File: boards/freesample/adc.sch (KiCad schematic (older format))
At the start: 20 parts, among them U41 DS25BR150, U8 HMC675LP3E

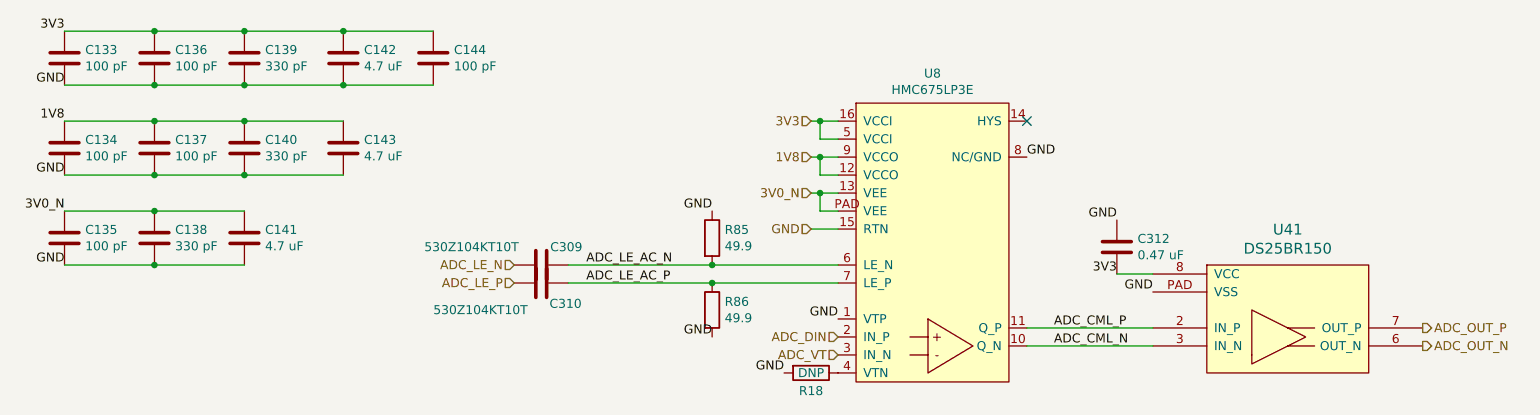
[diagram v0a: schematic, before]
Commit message: Added more test points. Started picking packages for passives. Continued schematic review.
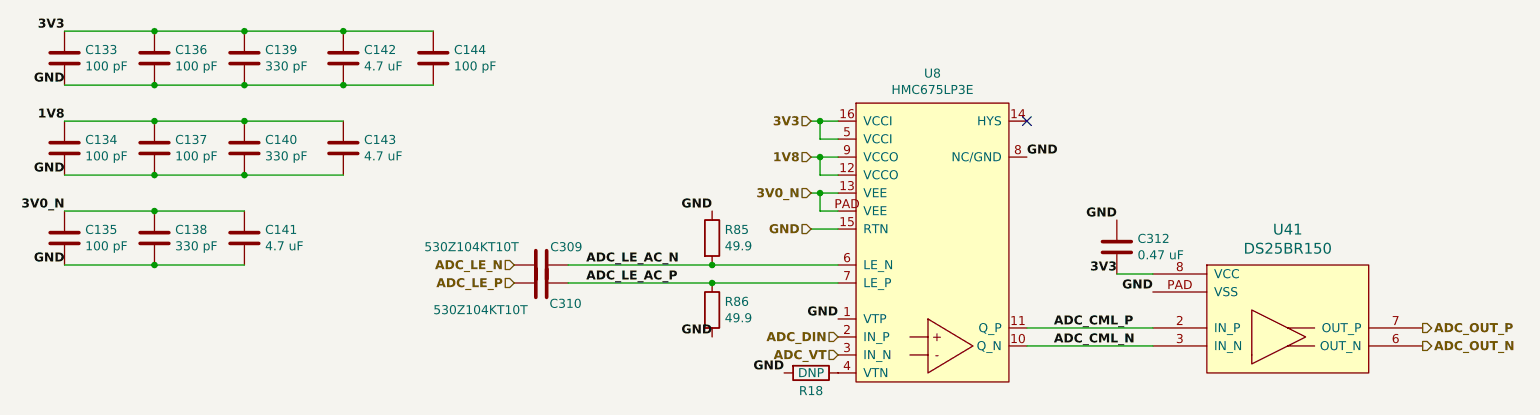
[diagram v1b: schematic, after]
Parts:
- C133, C134, C135, C136, C137, C138, C139, C140, C144, C309, C310: footprint (none) -> azonenberg_pcb:EIA_0201_CAP_NOSILK
- C141, C142, C143: footprint (none) -> azonenberg_pcb:EIA_0603_CAP_NOSILK
- C312: footprint (none) -> azonenberg_pcb:EIA_0402_CAP_NOSILK
- R18: footprint (none) -> azonenberg_pcb:EIA_0402_RES_NOSILK
- U41: footprint (none) -> azonenberg_pcb:DFN_8_0.5MM_3x3MM
- U8: footprint (none) -> azonenberg_pcb:QFN_16_0.5MM_3x3MM
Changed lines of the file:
@@
 Comment4 ""
 $EndDescr
-Text HLabel 5250 2550 0    50   Input ~ 0
+Text HLabel 5250 2550 0    50   Input ~ 6
 ADC_DIN
-Text HLabel 5250 2650 0    50   Input ~ 0
+Text HLabel 5250 2650 0    50   Input ~ 6
 ADC_VT
-Text HLabel 5100 1350 0    50   Input ~ 0
+Text HLabel 5100 1350 0    50   Input ~ 6
 3V3
-Text HLabel 5100 1750 0    50   Input ~ 0
+Text HLabel 5100 1750 0    50   Input ~ 6
 3V0_N
-Text HLabel 5100 1950 0    50   Input ~ 0
-GND
-Text HLabel 5100 1550 0    50   Input ~ 0
+Text HLabel 5100 1950 0    50   Input ~ 6
+GND
+Text HLabel 5100 1550 0    50   Input ~ 6
 1V8
-Text HLabel 8500 2500 2    50   Output ~ 0
+Text HLabel 8500 2500 2    50   Output ~ 6
 ADC_OUT_P
-Text HLabel 8500 2600 2    50   Output ~ 0
+Text HLabel 8500 2600 2    50   Output ~ 6
 ADC_OUT_N
-Text HLabel 3450 2250 0    50   Input ~ 0
+Text HLabel 3450 2250 0    50   Input ~ 6
 ADC_LE_P
-Text HLabel 3450 2150 0    50   Input ~ 0
+Text HLabel 3450 2150 0    50   Input ~ 6
 ADC_LE_N
 $Comp
@@
 F 0 "U8" H 5775 4515 50  0000 C CNN
 F 1 "HMC675LP3E" H 5775 4424 50  0000 C CNN
-F 2 "" H 5350 2800 50  0001 C CNN
+F 2 "azonenberg_pcb:QFN_16_0.5MM_3x3MM" H 5350 2800 50  0001 C CNN
 F 3 "" H 5350 2800 50  0001 C CNN
 	1    5350 2800
@@
 F 0 "C139" H 2065 1046 50  0000 L CNN
 F 1 "330 pF" H 2065 955 50  0000 L CNN
-F 2 "" H 1988 850 50  0001 C CNN
+F 2 "azonenberg_pcb:EIA_0201_CAP_NOSILK" H 1988 850 50  0001 C CNN
 F 3 "" H 1950 1000 50  0001 C CNN
 	1    1950 1000
@@
 F 0 "C136" H 1565 1046 50  0000 L CNN
 F 1 "100 pF" H 1565 955 50  0000 L CNN
-F 2 "" H 1488 850 50  0001 C CNN
+F 2 "azonenberg_pcb:EIA_0201_CAP_NOSILK" H 1488 850 50  0001 C CNN
 F 3 "" H 1450 1000 50  0001 C CNN
 	1    1450 1000
@@
 F 0 "C133" H 1065 1046 50  0000 L CNN
 F 1 "100 pF" H 1065 955 50  0000 L CNN
-F 2 "" H 988 850 50  0001 C CNN
+F 2 "azonenberg_pcb:EIA_0201_CAP_NOSILK" H 988 850 50  0001 C CNN
 F 3 "" H 950 1000 50  0001 C CNN
 	1    950  1000
 	1    0    0    -1
 $EndComp
-Text Label 950  1150 2    50   ~ 0
-GND
-Text Label 950  850  2    50   ~ 0
+Text Label 950  1150 2    50   ~ 6
+GND
+Text Label 950  850  2    50   ~ 6
 3V3
 $Comp
@@
 F 0 "C142" H 2615 1046 50  0000 L CNN
 F 1 "4.7 uF" H 2615 955 50  0000 L CNN
-F 2 "" H 2538 850 50  0001 C CNN
+F 2 "azonenberg_pcb:EIA_0603_CAP_NOSILK" H 2538 850 50  0001 C CNN
 F 3 "" H 2500 1000 50  0001 C CNN
 	1    2500 1000
@@
 F 0 "C144" H 3115 1046 50  0000 L CNN
 F 1 "100 pF" H 3115 955 50  0000 L CNN
-F 2 "" H 3038 850 50  0001 C CNN
+F 2 "azonenberg_pcb:EIA_0201_CAP_NOSILK" H 3038 850 50  0001 C CNN
 F 3 "" H 3000 1000 50  0001 C CNN
 	1    3000 1000
@@
 F 0 "C140" H 2065 1546 50  0000 L CNN
 F 1 "330 pF" H 2065 1455 50  0000 L CNN
-F 2 "" H 1988 1350 50  0001 C CNN
+F 2 "azonenberg_pcb:EIA_0201_CAP_NOSILK" H 1988 1350 50  0001 C CNN
 F 3 "" H 1950 1500 50  0001 C CNN
 	1    1950 1500
@@
 F 0 "C137" H 1565 1546 50  0000 L CNN
 F 1 "100 pF" H 1565 1455 50  0000 L CNN
-F 2 "" H 1488 1350 50  0001 C CNN
+F 2 "azonenberg_pcb:EIA_0201_CAP_NOSILK" H 1488 1350 50  0001 C CNN
 F 3 "" H 1450 1500 50  0001 C CNN
 	1    1450 1500
@@
 F 0 "C134" H 1065 1546 50  0000 L CNN
 F 1 "100 pF" H 1065 1455 50  0000 L CNN
-F 2 "" H 988 1350 50  0001 C CNN
+F 2 "azonenberg_pcb:EIA_0201_CAP_NOSILK" H 988 1350 50  0001 C CNN
 F 3 "" H 950 1500 50  0001 C CNN
 	1    950  1500
 	1    0    0    -1
 $EndComp
-Text Label 950  1650 2    50   ~ 0
-GND
-Text Label 950  1350 2    50   ~ 0
+Text Label 950  1650 2    50   ~ 6
+GND
+Text Label 950  1350 2    50   ~ 6
 1V8
 $Comp
@@
 F 0 "C143" H 2615 1546 50  0000 L CNN
 F 1 "4.7 uF" H 2615 1455 50  0000 L CNN
-F 2 "" H 2538 1350 50  0001 C CNN
+F 2 "azonenberg_pcb:EIA_0603_CAP_NOSILK" H 2538 1350 50  0001 C CNN
 F 3 "" H 2500 1500 50  0001 C CNN
 	1    2500 1500
@@
 Wire Wire Line
 	1950 1650 2500 1650
-Text Label 950  1850 2    50   ~ 0
+Text Label 950  1850 2    50   ~ 6
 3V0_N
 $Comp
@@
 F 0 "C135" H 1065 2046 50  0000 L CNN
 F 1 "100 pF" H 1065 1955 50  0000 L CNN
-F 2 "" H 988 1850 50  0001 C CNN
+F 2 "azonenberg_pcb:EIA_0201_CAP_NOSILK" H 988 1850 50  0001 C CNN
 F 3 "" H 950 2000 50  0001 C CNN
 	1    950  2000
@@
 F 0 "C138" H 1565 2046 50  0000 L CNN
 F 1 "330 pF" H 1565 1955 50  0000 L CNN
-F 2 "" H 1488 1850 50  0001 C CNN
+F 2 "azonenberg_pcb:EIA_0201_CAP_NOSILK" H 1488 1850 50  0001 C CNN
 F 3 "" H 1450 2000 50  0001 C CNN
 	1    1450 2000
@@
 F 0 "C141" H 2065 2046 50  0000 L CNN
 F 1 "4.7 uF" H 2065 1955 50  0000 L CNN
-F 2 "" H 1988 1850 50  0001 C CNN
+F 2 "azonenberg_pcb:EIA_0603_CAP_NOSILK" H 1988 1850 50  0001 C CNN
 F 3 "" H 1950 2000 50  0001 C CNN
 	1    1950 2000
@@
 Wire Wire Line
 	1450 2150 950  2150
-Text Label 950  2150 2    50   ~ 0
+Text Label 950  2150 2    50   ~ 6
 GND
 Wire Wire Line
@@
 Wire Wire Line
 	5150 1550 5250 1550
-Text Label 5250 2450 2    50   ~ 0
-GND
-Text Label 4950 2750 2    50   ~ 0
+Text Label 5250 2450 2    50   ~ 6
+GND
+Text Label 4950 2750 2    50   ~ 6
 GND
 $Comp
@@
 F 0 "R18" V 5200 2750 50  0000 C CNN
 F 1 "DNP" V 5100 2750 50  0000 C CNN
-F 2 "" V 5030 2750 50  0001 C CNN
+F 2 "azonenberg_pcb:EIA_0402_RES_NOSILK" V 5030 2750 50  0001 C CNN
 F 3 "" H 5100 2750 50  0001 C CNN
 	1    5100 2750
@@
 $EndComp
 NoConn ~ 6300 1350
-Text Label 6300 1550 0    50   ~ 0
+Text Label 6300 1550 0    50   ~ 6
 GND
 $Comp
@@
 F 0 "C309" V 3500 2200 50  0000 L CNN
 F 1 "530Z104KT10T" V 3500 1500 50  0000 L CNN
-F 2 "" H 3638 2000 50  0001 C CNN
+F 2 "azonenberg_pcb:EIA_0201_CAP_NOSILK" H 3638 2000 50  0001 C CNN
 F 3 "" H 3600 2150 50  0001 C CNN
 	1    3600 2150
@@
 F 0 "C310" V 3715 2296 50  0000 L CNN
 F 1 "530Z104KT10T" V 3750 1650 50  0000 L CNN
-F 2 "" H 3638 2100 50  0001 C CNN
+F 2 "azonenberg_pcb:EIA_0201_CAP_NOSILK" H 3638 2100 50  0001 C CNN
 F 3 "" H 3600 2250 50  0001 C CNN
 	1    3600 2250
@@
 Wire Wire Line
 	4550 2150 3750 2150
-Text Label 3850 2150 0    50   ~ 0
+Text Label 3850 2150 0    50   ~ 6
 ADC_LE_AC_N
-Text Label 3850 2250 0    50   ~ 0
+Text Label 3850 2250 0    50   ~ 6
 ADC_LE_AC_P
 $Comp
@@
 Wire Wire Line
 	3750 2250 4550 2250
-Text Label 4550 1850 2    50   ~ 0
+Text Label 4550 1850 2    50   ~ 6
 GND
 $Comp
@@
 Wire Wire Line
 	4550 2250 5250 2250
-Text Label 4550 2550 2    50   ~ 0
+Text Label 4550 2550 2    50   ~ 6
 GND
 $Comp
@@
 F 0 "U41" H 7750 3547 60  0000 C CNN
 F 1 "DS25BR150" H 7750 3441 60  0000 C CNN
-F 2 "" H 7300 2750 60  0001 C CNN
+F 2 "azonenberg_pcb:DFN_8_0.5MM_3x3MM" H 7300 2750 60  0001 C CNN
 F 3 "" H 7300 2750 60  0001 C CNN
 	1    7300 2750
 	1    0    0    -1
 $EndComp
-Text Label 6800 2200 2    50   ~ 0
+Text Label 6800 2200 2    50   ~ 6
 3V3
-Text Label 7000 2300 2    50   ~ 0
+Text Label 7000 2300 2    50   ~ 6
 GND
 $Comp
@@
 F 0 "C312" H 6915 2096 50  0000 L CNN
 F 1 "0.47 uF" H 6915 2005 50  0000 L CNN
-F 2 "" H 6838 1900 50  0001 C CNN
+F 2 "azonenberg_pcb:EIA_0402_CAP_NOSILK" H 6838 1900 50  0001 C CNN
 F 3 "" H 6800 2050 50  0001 C CNN
 	1    6800 2050
@@
 Wire Wire Line
 	6800 2200 7000 2200
-Text Label 6800 1900 2    50   ~ 0
+Text Label 6800 1900 2    50   ~ 6
 GND
 Wire Wire Line
@@
 Wire Wire Line
 	7000 2600 6300 2600
-Text Label 6450 2500 0    50   ~ 0
+Text Label 6450 2500 0    50   ~ 6
 ADC_CML_P
-Text Label 6450 2600 0    50   ~ 0
+Text Label 6450 2600 0    50   ~ 6
 ADC_CML_N
 $EndSCHEMATC

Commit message: Continued assigning footprints
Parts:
- R85, R86: footprint (none) -> azonenberg_pcb:EIA_0402_RES_NOSILK
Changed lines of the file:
@@
 Sheet 7 12
 Title "FREESAMPLE Oscilloscope"
-Date "2019-03-15"
+Date "2019-03-16"
 Rev "0.1"
 Comp "Andrew D. Zonenberg / Antikernel Labs"
@@
 F 0 "R85" H 4620 2046 50  0000 L CNN
 F 1 "49.9" H 4620 1955 50  0000 L CNN
-F 2 "" V 4480 2000 50  0001 C CNN
+F 2 "azonenberg_pcb:EIA_0402_RES_NOSILK" V 4480 2000 50  0001 C CNN
 F 3 "" H 4550 2000 50  0001 C CNN
 	1    4550 2000
@@
 F 0 "R86" H 4620 2446 50  0000 L CNN
 F 1 "49.9" H 4620 2355 50  0000 L CNN
-F 2 "" V 4480 2400 50  0001 C CNN
+F 2 "azonenberg_pcb:EIA_0402_RES_NOSILK" V 4480 2400 50  0001 C CNN
 F 3 "" H 4550 2400 50  0001 C CNN
 	1    4550 2400

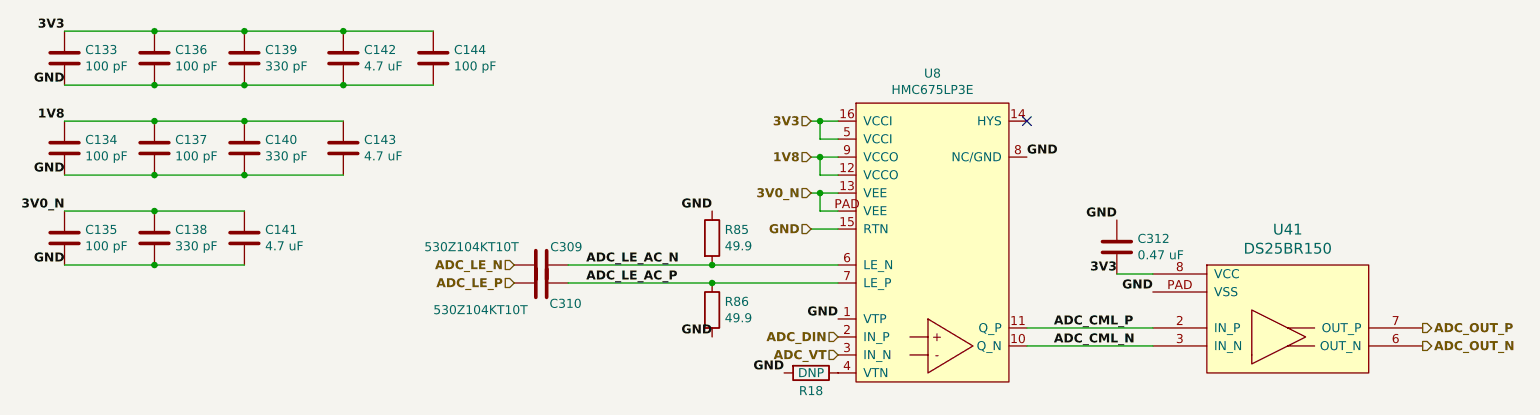
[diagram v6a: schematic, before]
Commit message: Finished initial layout of level trigger and ADC subsystems
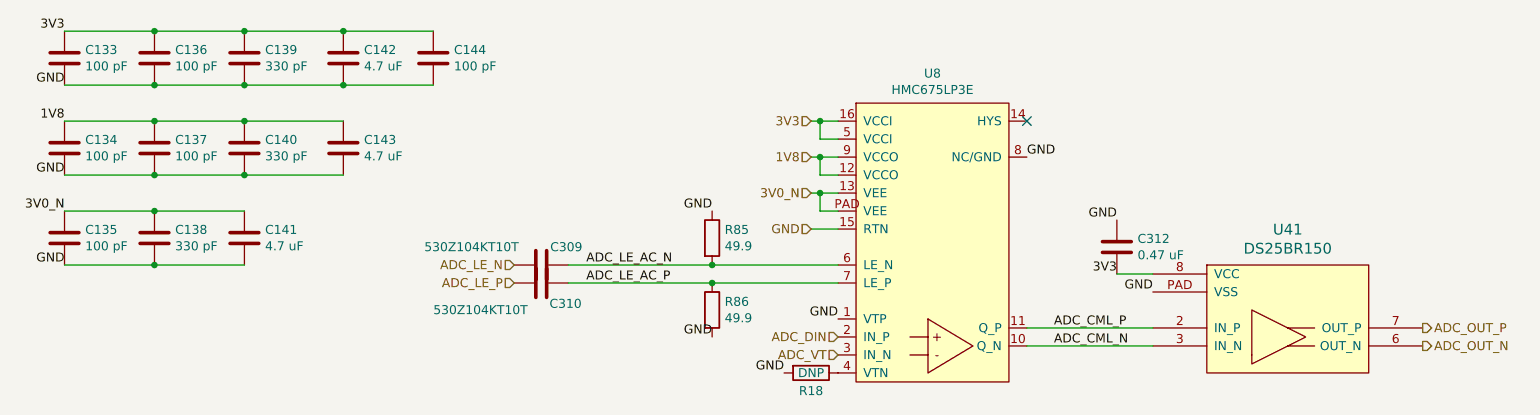
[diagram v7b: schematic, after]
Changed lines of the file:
@@
 Rev "0.1"
 Comp "Andrew D. Zonenberg / Antikernel Labs"
-Comment1 "Ready for review"
-Comment2 "Ready for review"
+Comment1 "A-D conversion"
+Comment2 "Layout in progress"
 Comment3 ""
 Comment4 ""
 $EndDescr
-Text HLabel 5250 2550 0    50   Input ~ 10
+Text HLabel 5250 2550 0    50   Input ~ 0
 ADC_DIN
-Text HLabel 5250 2650 0    50   Input ~ 10
+Text HLabel 5250 2650 0    50   Input ~ 0
 ADC_VT
-Text HLabel 5100 1350 0    50   Input ~ 10
+Text HLabel 5100 1350 0    50   Input ~ 0
 3V3
-Text HLabel 5100 1750 0    50   Input ~ 10
+Text HLabel 5100 1750 0    50   Input ~ 0
 3V0_N
-Text HLabel 5100 1950 0    50   Input ~ 10
-GND
-Text HLabel 5100 1550 0    50   Input ~ 10
+Text HLabel 5100 1950 0    50   Input ~ 0
+GND
+Text HLabel 5100 1550 0    50   Input ~ 0
 1V8
-Text HLabel 8500 2500 2    50   Output ~ 10
+Text HLabel 8500 2500 2    50   Output ~ 0
 ADC_OUT_P
-Text HLabel 8500 2600 2    50   Output ~ 10
+Text HLabel 8500 2600 2    50   Output ~ 0
 ADC_OUT_N
-Text HLabel 3450 2250 0    50   Input ~ 10
+Text HLabel 3450 2250 0    50   Input ~ 0
 ADC_LE_P
-Text HLabel 3450 2150 0    50   Input ~ 10
+Text HLabel 3450 2150 0    50   Input ~ 0
 ADC_LE_N
 $Comp
@@
 	1    0    0    -1
 $EndComp
-Text Label 950  1150 2    50   ~ 10
-GND
-Text Label 950  850  2    50   ~ 10
+Text Label 950  1150 2    50   ~ 0
+GND
+Text Label 950  850  2    50   ~ 0
 3V3
 $Comp
@@
 	1    0    0    -1
 $EndComp
-Text Label 950  1650 2    50   ~ 10
-GND
-Text Label 950  1350 2    50   ~ 10
+Text Label 950  1650 2    50   ~ 0
+GND
+Text Label 950  1350 2    50   ~ 0
 1V8
 $Comp
@@
 Wire Wire Line
 	1950 1650 2500 1650
-Text Label 950  1850 2    50   ~ 10
+Text Label 950  1850 2    50   ~ 0
 3V0_N
 $Comp
@@
 Wire Wire Line
 	1450 2150 950  2150
-Text Label 950  2150 2    50   ~ 10
+Text Label 950  2150 2    50   ~ 0
 GND
 Wire Wire Line
@@
 Wire Wire Line
 	5150 1550 5250 1550
-Text Label 5250 2450 2    50   ~ 10
-GND
-Text Label 4950 2750 2    50   ~ 10
+Text Label 5250 2450 2    50   ~ 0
+GND
+Text Label 4950 2750 2    50   ~ 0
 GND
 $Comp
@@
 $EndComp
 NoConn ~ 6300 1350
-Text Label 6300 1550 0    50   ~ 10
+Text Label 6300 1550 0    50   ~ 0
 GND
 $Comp
@@
 Wire Wire Line
 	4550 2150 3750 2150
-Text Label 3850 2150 0    50   ~ 10
+Text Label 3850 2150 0    50   ~ 0
 ADC_LE_AC_N
-Text Label 3850 2250 0    50   ~ 10
+Text Label 3850 2250 0    50   ~ 0
 ADC_LE_AC_P
 $Comp
@@
 Wire Wire Line
 	3750 2250 4550 2250
-Text Label 4550 1850 2    50   ~ 10
+Text Label 4550 1850 2    50   ~ 0
 GND
 $Comp
@@
 Wire Wire Line
 	4550 2250 5250 2250
-Text Label 4550 2550 2    50   ~ 10
+Text Label 4550 2550 2    50   ~ 0
 GND
 $Comp
@@
 	1    0    0    -1
 $EndComp
-Text Label 6800 2200 2    50   ~ 10
+Text Label 6800 2200 2    50   ~ 0
 3V3
-Text Label 7000 2300 2    50   ~ 10
+Text Label 7000 2300 2    50   ~ 0
 GND
 $Comp
@@
 Wire Wire Line
 	6800 2200 7000 2200
-Text Label 6800 1900 2    50   ~ 10
+Text Label 6800 1900 2    50   ~ 0
 GND
 Wire Wire Line
@@
 Wire Wire Line
 	7000 2600 6300 2600
-Text Label 6450 2500 0    50   ~ 10
+Text Label 6450 2500 0    50   ~ 0
 ADC_CML_P
-Text Label 6450 2600 0    50   ~ 10
+Text Label 6450 2600 0    50   ~ 0
 ADC_CML_N
 $EndSCHEMATC
